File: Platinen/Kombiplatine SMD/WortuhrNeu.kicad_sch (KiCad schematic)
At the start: 100 parts, among them J1 Conn_01x01_Pin, J2 PROG MODE, J3 UART FLOATING, J4 UART, J5 Eingangsbuchse, SW1 PTS645Vx83-2LFS, SW2 PTS645Vx83-2LFS, U2 MCP1826-ADJE/ET, U3 Bluepill, U4 DS18B20, U6 Arduino_Nano_Every, U7 ESP-07, U8 Generic DCDC, U9 TP582, X1 Conn_01x03_Pin, X10 Conn_01x03_Pin, X11 Conn_01x03_Pin, X12 Conn_01x03_Pin, X13 Conn_01x03_Pin, X14 Conn_01x03_Pin, X15 Conn_01x03_Pin, X16 Conn_01x03_Pin, X17 Conn_01x03_Pin, X18 Conn_01x03_Pin, X19 Conn_01x03_Pin, X2 Conn_01x03_Pin, X20 Conn_01x03_Pin, X21 Conn_01x03_Pin, X22 Conn_01x03_Pin, X23 Conn_01x03_Pin, X24 Conn_01x03_Pin, X25 Conn_01x03_Pin, X26 Conn_01x03_Pin, X27 Conn_01x03_Pin, X28 Conn_01x03_Pin, X29 Conn_01x03_Pin, X3 Conn_01x03_Pin, X30 Conn_01x03_Pin, X31 Conn_01x03_Pin, X32 Conn_01x03_Pin, X33 Conn_01x03_Pin, X34 Conn_01x03_Pin, X35 Conn_01x03_Pin, X36 Conn_01x03_Pin, X37 Conn_01x03_Pin, X38 Conn_01x03_Pin, X4 Conn_01x03_Pin, X5 Conn_01x03_Pin, X6 Conn_01x03_Pin, X7 Conn_01x03_Pin, X8 Conn_01x03_Pin, X9 Conn_01x03_Pin

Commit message: Implement some of the changes requested in issue 1
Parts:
- removed H8, H9: MountingHole, MountingHole:MountingHole_3.2mm_M3_DIN965, symbol Mechanical:MountingHole
- J1: footprint TestPoint:TestPoint_Pad_1.0x1.0mm -> Connector_PinHeader_1.00mm:PinHeader_1x01_P1.00mm_Vertical
- renumbered H7 to H5
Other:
- moved on the sheet: H2, H3, H6
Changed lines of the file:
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@@
 			)
 		)
-		(property "Footprint" "TestPoint:TestPoint_Pad_1.0x1.0mm"
+		(property "Footprint" "Connector_PinHeader_1.00mm:PinHeader_1x01_P1.00mm_Vertical"
 			(at 153.67 95.25 0)
 			(effects
@@
 		(dnp no)
 		(fields_autoplaced yes)
-		(property "Reference" "H7"
+		(property "Reference" "H5"
 			(at 170.18 293.3699 0)
 			(effects
@@
 			(project "WortuhrNeu"
 				(path "/9cd24a17-134e-4479-bc0b-dbbeb0113d4a"
-					(reference "H7")
+					(reference "H5")
 					(unit 1)
 				)
@@
 	)
 	(symbol
-		(lib_id "Mechanical:MountingHole")
-		(at 185.42 294.64 0)
-		(unit 1)
-		(exclude_from_sim yes)
-		(in_bom no)
-		(on_board yes)
-		(dnp no)
-		(property "Reference" "H9"
-			(at 187.96 293.3699 0)
-			(effects
-				(font
-					(size 1.27 1.27)
-				)
-				(justify left)
-			)
-		)
-		(property "Value" "MountingHole"
-			(at 187.96 295.9099 0)
-			(effects
-				(font
-					(size 1.27 1.27)
-				)
-				(justify left)
-				(hide yes)
-			)
-		)
-		(property "Footprint" "MountingHole:MountingHole_3.2mm_M3_DIN965"
-			(at 185.42 294.64 0)
-			(effects
-				(font
-					(size 1.27 1.27)
-				)
-				(hide yes)
-			)
-		)
-		(property "Datasheet" "~"
-			(at 185.42 294.64 0)
-			(effects
-				(font
-					(size 1.27 1.27)
-				)
-				(hide yes)
-			)
-		)
-		(property "Description" "Mounting Hole without connection"
-			(at 185.42 294.64 0)
-			(effects
-				(font
-					(size 1.27 1.27)
-				)
-				(hide yes)
-			)
-		)
-		(instances
-			(project "WortuhrNeu"
-				(path "/9cd24a17-134e-4479-bc0b-dbbeb0113d4a"
-					(reference "H9")
-					(unit 1)
-				)
-			)
-		)
-	)
-	(symbol
 		(lib_id "power:+5V")
 		(at 101.6 44.45 0)
@@
 	(symbol
 		(lib_id "Mechanical:MountingHole")
-		(at 158.75 294.64 0)
+		(at 179.07 294.64 0)
 		(unit 1)
 		(exclude_from_sim yes)
@@
 		(fields_autoplaced yes)
 		(property "Reference" "H6"
-			(at 161.29 293.3699 0)
+			(at 181.61 293.3699 0)
 			(effects
 				(font
@@
 		)
 		(property "Value" "MountingHole"
-			(at 161.29 295.9099 0)
+			(at 181.61 295.9099 0)
 			(effects
 				(font
@@
 		)
 		(property "Footprint" "MountingHole:MountingHole_3.2mm_M3_DIN965"
-			(at 158.75 294.64 0)
+			(at 179.07 294.64 0)
 			(effects
 				(font
@@
 		)
 		(property "Datasheet" "~"
-			(at 158.75 294.64 0)
+			(at 179.07 294.64 0)
 			(effects
 				(font
@@
 		)
 		(property "Description" "Mounting Hole without connection"
-			(at 158.75 294.64 0)
+			(at 179.07 294.64 0)
 			(effects
 				(font
@@
 	(symbol
 		(lib_id "Mechanical:MountingHole")
-		(at 157.48 66.04 0)
+		(at 138.43 72.39 0)
 		(unit 1)
 		(exclude_from_sim yes)
@@
 		(fields_autoplaced yes)
 		(property "Reference" "H2"
-			(at 160.02 64.7699 0)
+			(at 140.97 71.1199 0)
 			(effects
 				(font
@@
 		)
 		(property "Value" "MountingHole"
-			(at 160.02 67.3099 0)
+			(at 140.97 73.6599 0)
 			(effects
 				(font
@@
 		)
 		(property "Footprint" "MountingHole:MountingHole_3.2mm_M3_DIN965"
-			(at 157.48 66.04 0)
+			(at 138.43 72.39 0)
 			(effects
 				(font
@@
 		)
 		(property "Datasheet" "~"
-			(at 157.48 66.04 0)
+			(at 138.43 72.39 0)
 			(effects
 				(font
@@
 		)
 		(property "Description" "Mounting Hole without connection"
-			(at 157.48 66.04 0)
+			(at 138.43 72.39 0)
 			(effects
 				(font
@@
 	(symbol
 		(lib_id "Mechanical:MountingHole")
-		(at 173.99 69.85 0)
+		(at 190.5 72.39 0)
 		(unit 1)
 		(exclude_from_sim yes)
@@
 		(fields_autoplaced yes)
 		(property "Reference" "H3"
-			(at 176.53 68.5799 0)
+			(at 193.04 71.1199 0)
 			(effects
 				(font
@@
 		)
 		(property "Value" "MountingHole"
-			(at 176.53 71.1199 0)
+			(at 193.04 73.6599 0)
 			(effects
 				(font
@@
 		)
 		(property "Footprint" "MountingHole:MountingHole_3.2mm_M3_DIN965"
-			(at 173.99 69.85 0)
+			(at 190.5 72.39 0)
 			(effects
 				(font
@@
 		)
 		(property "Datasheet" "~"
-			(at 173.99 69.85 0)
+			(at 190.5 72.39 0)
 			(effects
 				(font
@@
 		)
 		(property "Description" "Mounting Hole without connection"
-			(at 173.99 69.85 0)
+			(at 190.5 72.39 0)
 			(effects
 				(font
@@
 					(unit 1)
 				)
-			)
-		)
-	)
-	(symbol
-		(lib_id "Mechanical:MountingHole")
-		(at 176.53 294.64 0)
-		(unit 1)
-		(exclude_from_sim yes)
-		(in_bom no)
-		(on_board yes)
-		(dnp no)
-		(fields_autoplaced yes)
-		(property "Reference" "H8"
-			(at 179.07 293.3699 0)
-			(effects
-				(font
-					(size 1.27 1.27)
-				)
-				(justify left)
-			)
-		)
-		(property "Value" "MountingHole"
-			(at 179.07 295.9099 0)
-			(effects
-				(font
-					(size 1.27 1.27)
-				)
-				(justify left)
-				(hide yes)
-			)
-		)
-		(property "Footprint" "MountingHole:MountingHole_3.2mm_M3_DIN965"
-			(at 176.53 294.64 0)
-			(effects
-				(font
-					(size 1.27 1.27)
-				)
-				(hide yes)
-			)
-		)
-		(property "Datasheet" "~"
-			(at 176.53 294.64 0)
-			(effects
-				(font
-					(size 1.27 1.27)
-				)
-				(hide yes)
-			)
-		)
-		(property "Description" "Mounting Hole without connection"
-			(at 176.53 294.64 0)
-			(effects
-				(font
-					(size 1.27 1.27)
-				)
-				(hide yes)
-			)
-		)
-		(instances
-			(project "WortuhrNeu"
-				(path "/9cd24a17-134e-4479-bc0b-dbbeb0113d4a"
-					(reference "H8")
-					(unit 1)
-				)

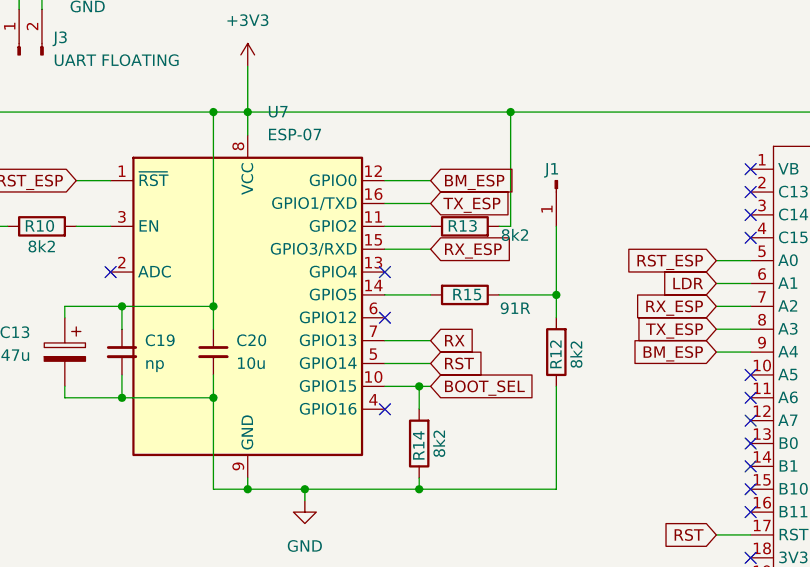
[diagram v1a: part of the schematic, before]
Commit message: Switched gpio4&5 on the esp for both boards
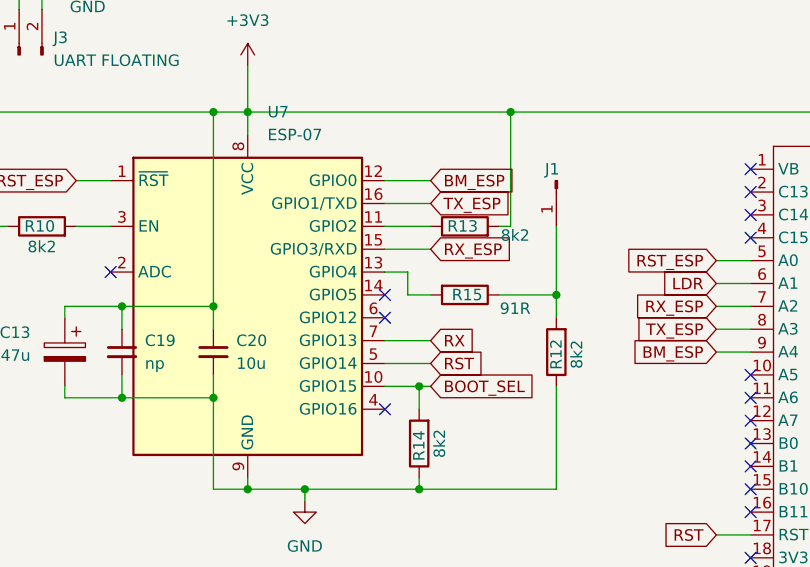
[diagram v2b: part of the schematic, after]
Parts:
- U5: value ~ -> (none)
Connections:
- net at R15.2: now also U7.13 (GPIO4); no longer U7.14 (GPIO5)
